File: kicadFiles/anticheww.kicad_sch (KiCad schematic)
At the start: 154 parts, among them J1 TYPE-C-31-M12_13, SW1 ESC, SW10 9, SW11 0, SW12 MINUS, SW13 PLUS, SW14 LBKSP, SW15 RBKSP, SW16 PGUP, SW17 2U_BKSP, SW18 TAB, SW19 Q, SW2 1, SW20 W, SW21 E, SW22 R, SW23 T, SW24 Y, SW25 U, SW26 I, SW27 O, SW28 P, SW29 LBRKT, SW3 2, SW30 RBRKT, SW31 BKSLSH, SW32 PGDN, SW33 CAPS, SW34 A, SW35 S, SW36 D, SW37 F, SW38 G, SW39 H, SW4 3, SW40 J, SW41 K, SW42 L, SW43 COLON, SW44 QUOTE, SW45 ENTER, SW46 HOME, SW47 LSHFT, SW48 STEPPED_CAPS, SW49 Z, SW5 4, SW50 X, SW51 C, SW52 V, SW53 B, SW54 N, SW55 M, SW56 COMMA, SW57 DOT, SW58 175_RSHFT, SW59 UP, SW6 5, SW60 END, SW61 SLSH, SW62 LCTRL, SW63 LGUI, SW64 LALT, SW65 SPC, SW66 RALT, SW67 RGUI, SW68 RCTRL, SW69 LEFT, SW7 6, SW70 DOWN, SW71 RIGHT, SW72 LCTRL, SW73 LGUI, SW74 LALT, SW75 SPC, SW8 7, SW9 8

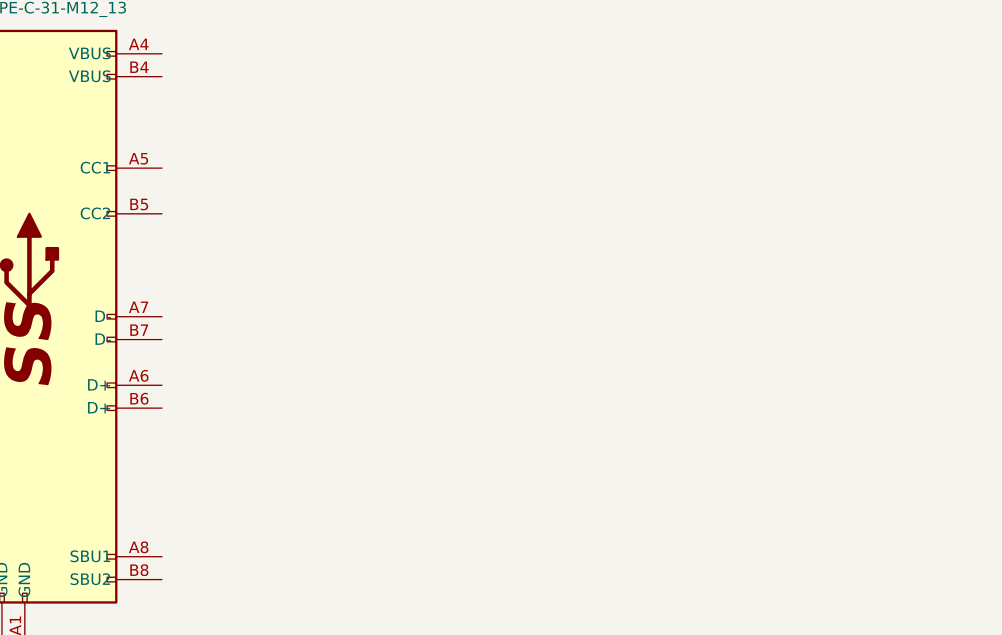
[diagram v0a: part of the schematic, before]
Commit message: Route USB data lines
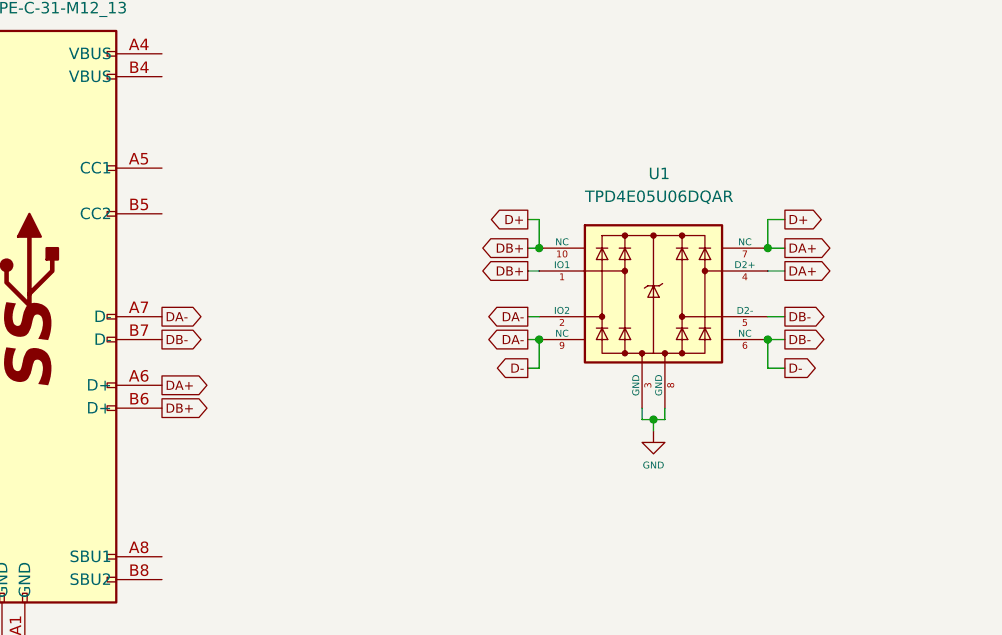
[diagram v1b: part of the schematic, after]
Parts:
- added U1: TPD4E05U06DQAR, acheron_Components:USON-10_2.5x1.0mm_P0.5mm, symbol acheronSymbols:TPD4E05U06DQAR
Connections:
- net GND: now also U1.3 (GND), U1.8 (GND)
- net D+: now reaches J1.A6 (D+)
- net D+: now also J1.B6 (D+), U1.1 (IO1), U1.10 (NC), U1.4 (D2+), U1.7 (NC)
- net D-: now reaches J1.A7 (D-)
- net D-: now also J1.B7 (D-), U1.2 (IO2), U1.5 (D2-), U1.6 (NC), U1.9 (NC)
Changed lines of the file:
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@@
     (title "Anticheww")
     (date "2020-07-03")
-    (rev "V2.0.1")
+    (rev "V2.0.2")
     (company "Designed by Gondolindrim")
     (comment 1 "In partnership with Chewwy")
@@
   (junction (at 127 118.11) (diameter 0) (color 0 0 0 0))
   (junction (at 153.035 548.005) (diameter 0) (color 0 0 0 0))
+  (junction (at 211.455 502.285) (diameter 0) (color 0 0 0 0))
+  (junction (at 211.455 512.445) (diameter 0) (color 0 0 0 0))
+  (junction (at 224.155 521.335) (diameter 0) (color 0 0 0 0))
+  (junction (at 236.855 502.285) (diameter 0) (color 0 0 0 0))
+  (junction (at 236.855 512.445) (diameter 0) (color 0 0 0 0))
   (junction (at 482.6 54.61) (diameter 0) (color 0 0 0 0))
   (wire (pts (xy 118.11 127) (xy 118.11 128.27))
@@
     (stroke (width 0) (type solid) (color 0 0 0 0))
   )
+  (wire (pts (xy 210.185 499.11) (xy 211.455 499.11))
+    (stroke (width 0) (type solid) (color 0 0 0 0))
+  )
+  (wire (pts (xy 210.185 502.285) (xy 211.455 502.285))
+    (stroke (width 0) (type solid) (color 0 0 0 0))
+  )
+  (wire (pts (xy 210.185 504.825) (xy 211.455 504.825))
+    (stroke (width 0) (type solid) (color 0 0 0 0))
+  )
+  (wire (pts (xy 210.185 509.905) (xy 211.455 509.905))
+    (stroke (width 0) (type solid) (color 0 0 0 0))
+  )
+  (wire (pts (xy 210.185 512.445) (xy 211.455 512.445))
+    (stroke (width 0) (type solid) (color 0 0 0 0))
+  )
+  (wire (pts (xy 211.455 499.11) (xy 211.455 502.285))
+    (stroke (width 0) (type solid) (color 0 0 0 0))
+  )
+  (wire (pts (xy 211.455 512.445) (xy 211.455 515.62))
+    (stroke (width 0) (type solid) (color 0 0 0 0))
+  )
+  (wire (pts (xy 211.455 515.62) (xy 210.185 515.62))
+    (stroke (width 0) (type solid) (color 0 0 0 0))
+  )
+  (wire (pts (xy 222.885 520.065) (xy 222.885 521.335))
+    (stroke (width 0) (type solid) (color 0 0 0 0))
+  )
+  (wire (pts (xy 222.885 521.335) (xy 224.155 521.335))
+    (stroke (width 0) (type solid) (color 0 0 0 0))
+  )
+  (wire (pts (xy 224.155 521.335) (xy 224.155 522.605))
+    (stroke (width 0) (type solid) (color 0 0 0 0))
+  )
+  (wire (pts (xy 224.155 521.335) (xy 225.425 521.335))
+    (stroke (width 0) (type solid) (color 0 0 0 0))
+  )
+  (wire (pts (xy 225.425 521.335) (xy 225.425 520.065))
+    (stroke (width 0) (type solid) (color 0 0 0 0))
+  )
   (wire (pts (xy 228.6 44.45) (xy 228.6 45.72))
     (stroke (width 0) (type solid) (color 0 0 0 0))
@@
     (stroke (width 0) (type solid) (color 0 0 0 0))
   )
+  (wire (pts (xy 236.855 499.11) (xy 236.855 502.285))
+    (stroke (width 0) (type solid) (color 0 0 0 0))
+  )
+  (wire (pts (xy 236.855 502.285) (xy 238.76 502.285))
+    (stroke (width 0) (type solid) (color 0 0 0 0))
+  )
+  (wire (pts (xy 236.855 504.825) (xy 238.76 504.825))
+    (stroke (width 0) (type solid) (color 0 0 0 0))
+  )
+  (wire (pts (xy 236.855 509.905) (xy 238.76 509.905))
+    (stroke (width 0) (type solid) (color 0 0 0 0))
+  )
+  (wire (pts (xy 236.855 512.445) (xy 238.76 512.445))
+    (stroke (width 0) (type solid) (color 0 0 0 0))
+  )
+  (wire (pts (xy 236.855 515.62) (xy 236.855 512.445))
+    (stroke (width 0) (type solid) (color 0 0 0 0))
+  )
+  (wire (pts (xy 238.76 499.11) (xy 236.855 499.11))
+    (stroke (width 0) (type solid) (color 0 0 0 0))
+  )
+  (wire (pts (xy 238.76 515.62) (xy 236.855 515.62))
+    (stroke (width 0) (type solid) (color 0 0 0 0))
+  )
   (wire (pts (xy 254 44.45) (xy 254 45.72))
     (stroke (width 0) (type solid) (color 0 0 0 0))
@@
     (effects (font (size 1.27 1.27)) (justify left))
   )
+  (global_label "DA-" (shape output) (at 169.545 509.905 0)
+    (effects (font (size 1.016 1.016)) (justify left))
+  )
+  (global_label "DB-" (shape output) (at 169.545 512.445 0)
+    (effects (font (size 1.016 1.016)) (justify left))
+  )
+  (global_label "DA+" (shape output) (at 169.545 517.525 0)
+    (effects (font (size 1.016 1.016)) (justify left))
+  )
+  (global_label "DB+" (shape output) (at 169.545 520.065 0)
+    (effects (font (size 1.016 1.016)) (justify left))
+  )
+  (global_label "D+" (shape output) (at 210.185 499.11 180)
+    (effects (font (size 1.016 1.016)) (justify right))
+  )
+  (global_label "DB+" (shape output) (at 210.185 502.285 180)
+    (effects (font (size 1.016 1.016)) (justify right))
+  )
+  (global_label "DB+" (shape output) (at 210.185 504.825 180)
+    (effects (font (size 1.016 1.016)) (justify right))
+  )
+  (global_label "DA-" (shape output) (at 210.185 509.905 180)
+    (effects (font (size 1.016 1.016)) (justify right))
+  )
+  (global_label "DA-" (shape output) (at 210.185 512.445 180)
+    (effects (font (size 1.016 1.016)) (justify right))
+  )
+  (global_label "D-" (shape output) (at 210.185 515.62 180)
+    (effects (font (size 1.016 1.016)) (justify right))
+  )
+  (global_label "D+" (shape output) (at 238.76 499.11 0)
+    (effects (font (size 1.016 1.016)) (justify left))
+  )
+  (global_label "DA+" (shape output) (at 238.76 502.285 0)
+    (effects (font (size 1.016 1.016)) (justify left))
+  )
+  (global_label "DA+" (shape output) (at 238.76 504.825 0)
+    (effects (font (size 1.016 1.016)) (justify left))
+  )
+  (global_label "DB-" (shape output) (at 238.76 509.905 0)
+    (effects (font (size 1.016 1.016)) (justify left))
+  )
+  (global_label "DB-" (shape output) (at 238.76 512.445 0)
+    (effects (font (size 1.016 1.016)) (justify left))
+  )
+  (global_label "D-" (shape output) (at 238.76 515.62 0)
+    (effects (font (size 1.016 1.016)) (justify left))
+  )
   (symbol (lib_id "power:GND") (at 153.035 549.275 0) (unit 1)
     (in_bom yes) (on_board yes)
@@
     )
   )
+  (symbol (lib_id "power:GND") (at 224.155 522.605 0) (unit 1)
+    (in_bom yes) (on_board yes)
+    (property "Reference" "#PWR0102" (id 0) (at 224.155 528.955 0)
+      (effects (font (size 1.27 1.27)) hide)
+    )
+    (property "Value" "GND" (id 1) (at 224.155 526.415 0)
+      (effects (font (size 0.762 0.762)))
+    )
+    (property "Footprint" "" (id 2) (at 224.155 522.605 0)
+      (effects (font (size 1.27 1.27)) hide)
+    )
+    (property "Datasheet" "" (id 3) (at 224.155 522.605 0)
+      (effects (font (size 1.27 1.27)) hide)
+    )
+  )
   (symbol (lib_id "Mechanical:MountingHole") (at 71.12 495.935 0) (unit 1)
     (in_bom no) (on_board yes)
@@
     )
   )
+  (symbol (lib_id "acheronSymbols:TPD4E05U06DQAR") (at 224.155 507.365 0) (unit 1)
+    (in_bom yes) (on_board yes)
+    (property "Reference" "U1" (id 0) (at 224.79 494.03 0))
+    (property "Value" "TPD4E05U06DQAR" (id 1) (at 224.79 496.57 0))
+    (property "Footprint" "acheron_Components:USON-10_2.5x1.0mm_P0.5mm" (id 2) (at 224.155 480.695 0)
+      (effects (font (size 1.27 1.27)) hide)
+    )
+    (property "Datasheet" "" (id 3) (at 224.155 507.365 0)
+      (effects (font (size 1.27 1.27)) hide)
+    )
+    (property "Manufacturer" "Texas Instruments" (id 4) (at 224.155 483.235 0)
+      (effects (font (size 1.27 1.27)) hide)
+    )
+    (property "Package" "uSON-10" (id 7) (at 224.155 485.775 0)
+      (effects (font (size 1.27 1.27)) hide)
+    )
+    (property "Manufacturer Part Number" "TPD4E05U06DQAR" (id 4) (at 224.155 507.365 0)
+      (effects (font (size 1.27 1.27)) hide)
+    )
+    (property "LCSC Part Number" "C138714" (id 5) (at 224.155 507.365 0)
+      (effects (font (size 1.27 1.27)) hide)
+    )
+  )
   (symbol (lib_id "acheronSymbols:TYPE-C-31-M12_13") (at 154.305 509.905 0) (unit 1)
     (in_bom yes) (on_board yes)
@@
       (reference "#PWR0101") (unit 1)
     )
+    (path "/2ca7166e-cb5d-4fa3-b1b6-95a762aabfb3"
+      (reference "#PWR0102") (unit 1)
+    )
     (path "/543a7d54-a886-4795-b487-5ed8576a1063"
       (reference "D1") (unit 1)
@@
       (reference "SW75") (unit 1)
     )
+    (path "/155bad83-d77a-43be-9512-7c5efecea63e"
+      (reference "U1") (unit 1)
+    )
   )

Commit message: Add RGB
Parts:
- added C1, C10, C11, C12, C13, C14, C2, C3, C4, C5, C6, C7, C8, C9: 100n, Capacitor_SMD:C_0805_2012Metric, symbol Device:C
- added D47: 1N4148W, acheron_Components:D_SOD-123, symbol Device:D
- added D71, D72, D73, D74, D75, D76, D77, D78, D79, D80, D81, D82, D83, D84: WS2812C, acheron_Components:LED_WS2812B_5.0x5.0mm_P3.2mm, symbol LED:WS2812B
- added FB1, FB2: CBG201209U121T, Inductor_SMD:L_0805_2012Metric, symbol Device:Ferrite_Bead_Small
- added GR1: Warning Sign (ISO Enter + LED), acheron_Graphics:warning_sign_3.6x3.2mm, symbol Mechanical:MountingHole
- added GR2: Warning Sign (Backspace), acheron_Graphics:warning_sign_3.6x3.2mm, symbol Mechanical:MountingHole
- added GR3: Warning Sign (ANSI Enter + ISO Backslash), acheron_Graphics:warning_sign_3.6x3.2mm, symbol Mechanical:MountingHole
- added GR4: Warning Sign (7U Space), acheron_Graphics:warning_sign_3.6x3.2mm, symbol Mechanical:MountingHole
- added GR5: Warning Sign (Left shift), acheron_Graphics:warning_sign_3.6x3.2mm, symbol Mechanical:MountingHole
- added LED1, LED10, LED11, LED12, LED13, LED14, LED15, LED16, LED17, LED18, LED19, LED2, LED20, LED21, LED22, LED23, LED24, LED25, LED26, LED27, LED28, LED29, LED3, LED30, LED31, LED32, LED33, LED34, LED35, LED36, LED37, LED38, LED39, LED4, LED40, LED41, LED42, LED43, LED44, LED45, LED46, LED47, LED48, LED49, LED5, LED50, LED51, LED52, LED53, LED54, LED55, LED56, LED57, LED58, LED59, LED6, LED60, LED61, LED62, LED63, LED64, LED65, LED66, LED67, LED68, LED69, LED7, LED70, LED71, LED72, LED73, LED74, LED75, LED76, LED77, LED78, LED79, LED8, LED80, LED9: LED, acheron_Components:LED_THT_2.54mm, symbol acheronSymbols:LED
- added Q1: AO3401A, Package_TO_SOT_SMD:SOT-23, symbol Transistor_FET:AO3401A
- added Q2: DTC123JKAT146, Package_TO_SOT_SMD:SOT-23, symbol acheronSymbols:DTC123J
- added R1: 1k, Resistor_SMD:R_0805_2012Metric, symbol Device:R
- added R10, R11, R12, R13, R14, R15, R16, R17, R18, R19, R20, R21, R22, R23, R24, R25, R33, R34, R35, R36, R37, R38, R39, R40, R41, R42, R43, R44, R45, R46, R47, R48, R49, R50, R51, R52, R53, R54, R55, R56, R57, R58, R59, R60, R61, R62, R63, R64, R65, R66, R67, R68, R69, R70, R71, R72, R73, R74, R75, R76, R77, R78, R79, R80, R81, R82, R83, R84, R85, R86, R87, R88, R89: 420R, Resistor_SMD:R_0805_2012Metric, symbol Device:R
- added R2: 100R, Resistor_SMD:R_0805_2012Metric, symbol Device:R
- added R26, R27, R28, R29, R3, R30, R31, R32, R4, R5, R6, R7, R8, R9: 5R, Resistor_SMD:R_0805_2012Metric, symbol Device:R
- added R90, R91: 5.1k, Resistor_SMD:R_0805_2012Metric, symbol Device:R
- added SW32: ISO_ENTER, acheron_MX_SolderMask:MX_ISOEnter_Vertical_LED, symbol acheronSymbols:MXSwitch
- added SW49: ISO_TILDE, acheron_MX_SolderMask:MX100, symbol acheronSymbols:MXSwitch
- added SW51: ISO_BKLSH, acheron_MX_SolderMask:MX100, symbol acheronSymbols:MXSwitch
- added SW65: ISO_LSHFT, acheron_MX_SolderMask:MX125, symbol acheronSymbols:MXSwitch
- H1: renamed from H2; symbol Mechanical:MountingHole -> Mechanical:MountingHole_Pad
- H7: renamed from H8; symbol Mechanical:MountingHole_Pad -> Mechanical:MountingHole
- SW45: footprint acheron_MX_SolderMask:MX225R -> acheron_MX_SolderMask:MX225
- U1: Manufacturer Texas Instruments -> (none); Package uSON-10 -> (none)
- renumbered D17 to D16, D18 to D17, D19 to D18, D20 to D19, D21 to D20, D22 to D21, D23 to D22, D24 to D23, D25 to D24, D26 to D25, D27 to D26, D28 to D27, D29 to D28, D30 to D29, D31 to D30, D32 to D31, D33 to D32, D34 to D33, D35 to D34, D36 to D35, D37 to D36, D38 to D37, D39 to D38, D40 to D39, D41 to D40, D42 to D41, D43 to D42, D44 to D43, D45 to D44, D16 to D45, D47 to D48, D48 to D49, D49 to D50, D50 to D51, D51 to D52, D52 to D53, D53 to D54, D54 to D55, D55 to D56, D59 to D57, D56 to D58, D57 to D59, D58 to D60, D60 to D61, D61 to D62, D62 to D63, D63 to D64, D64 to D65, D65 to D66, D66 to D67, D67 to D68, D68 to D69, D69 to D70, H3 to H2, H4 to H3, H5 to H4, H6 to H5, H7 to H6, H9 to H8, H10 to H9, SW17 to SW16, SW18 to SW17, SW19 to SW18, SW20 to SW19, SW21 to SW20, SW22 to SW21, SW23 to SW22, SW24 to SW23, SW25 to SW24, SW26 to SW25, SW27 to SW26, SW28 to SW27, SW29 to SW28, SW30 to SW29, SW31 to SW30, SW32 to SW31, SW16 to SW47, SW47 to SW50, SW49 to SW52, SW50 to SW53, SW51 to SW54, SW52 to SW55, SW53 to SW56, SW54 to SW57, SW55 to SW58, SW56 to SW59, SW57 to SW60, SW58 to SW62, SW59 to SW63, SW60 to SW64, SW62 to SW66, SW63 to SW67, SW64 to SW68, SW65 to SW69, SW66 to SW70, SW67 to SW71, SW68 to SW72, SW69 to SW73, SW70 to SW74, SW71 to SW75, SW72 to SW76, SW73 to SW77, SW74 to SW78, SW75 to SW79
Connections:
- net CASE: now also H1.1, FB1.2; no longer H7.1
- net GND: now also C1.1, C10.1, C11.1, C12.1, C13.1, C14.1, C2.1, C3.1, C4.1, C5.1, C6.1, C7.1, C8.1, C9.1, D71.3 (VSS), D72.3 (VSS), D73.3 (VSS), D74.3 (VSS), D75.3 (VSS), D76.3 (VSS), D77.3 (VSS), D78.3 (VSS), D79.3 (VSS), D80.3 (VSS), D81.3 (VSS), D82.3 (VSS), D83.3 (VSS), D84.3 (VSS), FB1.1, FB2.1, LED1.K, LED10.K, LED11.K, LED12.K, LED13.K, LED14.K, LED15.K, LED16.K, LED17.K, LED18.K, LED19.K, LED2.K, LED20.K, LED21.K, LED22.K, LED23.K, LED24.K, LED25.K, LED26.K, LED27.K, LED28.K, LED29.K, LED3.K, LED30.K, LED31.K, LED32.K, LED33.K, LED34.K, LED35.K, LED36.K, LED37.K, LED38.K, LED39.K, LED4.K, LED40.K, LED41.K, LED42.K, LED43.K, LED44.K, LED45.K, LED46.K, LED47.K, LED48.K, LED49.K, LED5.K, LED50.K, LED51.K, LED52.K, LED53.K, LED54.K, LED55.K, LED56.K, LED57.K, LED58.K, LED59.K, LED6.K, LED60.K, LED61.K, LED62.K, LED63.K, LED64.K, LED65.K, LED66.K, LED67.K, LED68.K, LED69.K, LED7.K, LED70.K, LED71.K, LED72.K, LED73.K, LED74.K, LED75.K, LED76.K, LED77.K, LED78.K, LED79.K, LED8.K, LED80.K, LED9.K, Q2.2 (E), R90.2, R91.2
- net at D5.1 (K): now also D1.1 (K), D10.1 (K), D11.1 (K), D12.1 (K), D13.1 (K), D14.1 (K), D15.1 (K), D2.1 (K), D3.1 (K), D4.1 (K), D6.1 (K), D7.1 (K), D8.1 (K), D9.1 (K)
- net at SW18.1 (Col): now also SW2.1 (Col), SW34.1 (Col), SW67.1 (Col), SW77.1 (Col), SW51.1 (Col)
- net at D17.1 (K): now also D16.1 (K), D18.1 (K), D19.1 (K), D20.1 (K), D21.1 (K), D22.1 (K), D23.1 (K), D24.1 (K), D25.1 (K), D26.1 (K), D27.1 (K), D28.1 (K), D29.1 (K), D30.1 (K)
- net at SW14.1 (Col): now also SW30.1 (Col), SW46.1 (Col), SW63.1 (Col), SW74.1 (Col), SW32.1 (Col)
- net at D31.1 (K): now also D32.1 (K), D33.1 (K), D34.1 (K), D35.1 (K), D36.1 (K), D37.1 (K), D38.1 (K), D39.1 (K), D40.1 (K), D41.1 (K), D42.1 (K), D43.1 (K), D44.1 (K), D45.1 (K)
- net at SW78.1 (Col): now also SW19.1 (Col), SW3.1 (Col), SW35.1 (Col), SW52.1 (Col), SW68.1 (Col)
- net S3: now reaches SW78.2 (Row)
- net S3: now also D63.2 (A), SW68.2 (Row)
- net at SW22.1 (Col): now also SW38.1 (Col), SW55.1 (Col), SW6.1 (Col), SW69.1 (Col), SW79.1 (Col)
- net at D29.2 (A), SW30.2 (Row): now also SW32.2 (Row)
- net at SW12.1 (Col): now also SW28.1 (Col), SW44.1 (Col), SW61.1 (Col), SW72.1 (Col)
- net at SW75.1 (Col): now also SW15.1 (Col), SW16.1 (Col), SW31.1 (Col), SW47.1 (Col), SW64.1 (Col)
- net at SW56.1 (Col): now also SW23.1 (Col), SW39.1 (Col), SW7.1 (Col)
- net at SW24.1 (Col): now also SW40.1 (Col), SW57.1 (Col), SW8.1 (Col)
- net at SW27.1 (Col): now also SW11.1 (Col), SW43.1 (Col), SW60.1 (Col), SW71.1 (Col)
- net at D70.1 (K): now also D61.1 (K), D62.1 (K), D63.1 (K), D64.1 (K), D65.1 (K), D66.1 (K), D67.1 (K), D68.1 (K), D69.1 (K)
- net at D48.1 (K): now also D46.1 (K), D49.1 (K), D50.1 (K), D51.1 (K), D52.1 (K), D53.1 (K), D54.1 (K), D55.1 (K), D56.1 (K), D57.1 (K), D58.1 (K), D59.1 (K), D60.1 (K), D47.1 (K)
- net at SW37.1 (Col): now also SW21.1 (Col), SW5.1 (Col), SW54.1 (Col)
- net S4: now reaches SW79.2 (Row)
- net S4: now also D64.2 (A), SW69.2 (Row)
- net VBUS: now reaches J1.A4 (VBUS)
- net VBUS: now also J1.B4 (VBUS)
- net at J1.A5 (CC1): now also R90.1
- net at J1.B5 (CC2): now also R91.1
- net at J1.S (SHIELD): now also FB2.2
- net at SW25.1 (Col): now also SW41.1 (Col), SW58.1 (Col), SW9.1 (Col)
- net S2: now reaches SW77.2 (Row)
- net S2: now also D62.2 (A), SW67.2 (Row)
- net at SW29.1 (Col): now also SW13.1 (Col), SW45.1 (Col), SW62.1 (Col), SW73.1 (Col), SW49.1 (Col)
- net at SW4.1 (Col): now also SW20.1 (Col), SW36.1 (Col), SW53.1 (Col)
- net S1: now reaches D61.2 (A), SW66.2 (Row)
- net S1: now also SW76.2 (Row)
- net at SW66.1 (Col): now also SW1.1 (Col), SW17.1 (Col), SW33.1 (Col), SW48.1 (Col), SW50.1 (Col), SW76.1 (Col), SW65.1 (Col)
- net at SW70.1 (Col): now also SW10.1 (Col), SW26.1 (Col), SW42.1 (Col), SW59.1 (Col)
- net at D46.2 (A), SW50.2 (Row): now also SW65.2 (Row)
- net at D43.2 (A), SW45.2 (Row): now also SW49.2 (Row)
- new net: LED61.A, R74.1
- new net: Q1.3 (D), R10.2, R11.2, R12.2, R13.2, R14.2, R15.2, R16.2, R17.2, R18.2, R19.2, R20.2, R21.2, R22.2, R23.2, R24.2, R25.2, R33.2, R34.2, R35.2, R36.2, R37.2, R38.2, R39.2, R40.2, R41.2, R42.2, R43.2, R44.2, R45.2, R46.2, R47.2, R48.2, R49.2, R50.2, R51.2, R52.2, R53.2, R54.2, R55.2, R56.2, R57.2, R58.2, R59.2, R60.2, R61.2, R62.2, R63.2, R64.2, R65.2, R66.2, R67.2, R68.2, R69.2, R70.2, R71.2, R72.2, R73.2, R74.2, R75.2, R76.2, R77.2, R78.2, R79.2, R80.2, R81.2, R82.2, R83.2, R84.2, R85.2, R86.2, R87.2, R88.2, R89.2
- new net: LED48.A, R62.1
- new net: LED7.A, R16.1
- new net: LED19.A, R34.1
- new net: LED14.A, R23.1
- new net: C2.2, D72.1 (VDD), R4.1
- new net: LED46.A, R60.1
- new net: C14.2, D84.1 (VDD), R32.1
- new net: LED37.A, R51.1
- new net: C7.2, D77.1 (VDD), R9.1
- new net: C5.2, D75.1 (VDD), R7.1
- new net: LED33.A, LED34.A, R48.1
- new net: LED60.A, R73.1
- new net: LED30.A, R45.1
- new net: D72.2 (DOUT), D73.4 (DIN)
- new net: D71.2 (DOUT), D72.4 (DIN)
- new net: LED31.A, R46.1
- new net: LED39.A, R53.1
- new net: LED15.A, LED16.A, R24.1
- new net: LED43.A, R57.1
- new net: LED57.A, R70.1
- new net: LED17.A, R25.1
- new net: LED67.A, LED68.A, R79.1
- new net: LED65.A, LED66.A, R78.1
- new net: LED78.A, R87.1
- new net: LED22.A, R37.1
- new net: C10.2, D80.1 (VDD), R28.1
- new net: D79.4 (DIN), D80.2 (DOUT)
- new net: D80.4 (DIN), D81.2 (DOUT)
- new net: LED53.A, R66.1
- new net: Q2.3 (C), R1.2, R2.2
- new net: LED6.A, R15.1
- new net: LED74.A, R83.1
- new net: LED18.A, R33.1
- new net: LED62.A, R75.1
- new net: LED69.A, LED70.A, R80.1
- new net: LED10.A, R19.1
- new net: LED27.A, R42.1
- new net: LED29.A, R44.1
- new net: C8.2, D78.1 (VDD), R26.1
- new net: D78.4 (DIN), D79.2 (DOUT)
- new net: LED8.A, R17.1
- new net: C13.2, D83.1 (VDD), R31.1
- new net: C3.2, D73.1 (VDD), R5.1
- new net: LED71.A, LED72.A, R81.1
- new net: LED80.A, R89.1
- new net: LED44.A, R58.1
- new net: LED24.A, R39.1
- new net: Q1.1 (G), R2.1
- new net: LED4.A, R13.1
- new net: LED9.A, R18.1
- new net: LED77.A, R86.1
- new net: LED59.A, R72.1
- new net: LED23.A, R38.1
- new net: LED45.A, R59.1
- new net: LED40.A, R54.1
- new net: C12.2, D82.1 (VDD), R30.1
- new net: D81.4 (DIN), D82.2 (DOUT)
- new net: D82.4 (DIN), D83.2 (DOUT)
- new net: LED3.A, R12.1
- new net: LED26.A, R41.1
- new net: LED54.A, R67.1
- new net: LED55.A, R68.1
- new net: C11.2, D81.1 (VDD), R29.1
- new net: D83.4 (DIN), D84.2 (DOUT)
- new net: D77.2 (DOUT), D84.4 (DIN)
- new net: LED56.A, R69.1
- new net: LED11.A, R20.1
- new net: LED25.A, R40.1
- new net: LED49.A, LED50.A, R63.1
- new net: LED64.A, R77.1
- new net: LED42.A, R56.1
- new net: C6.2, D76.1 (VDD), R8.1
- new net: LED5.A, R14.1
- new net: LED32.A, R47.1
- new net: C9.2, D79.1 (VDD), R27.1
- new net: LED73.A, R82.1
- new net: LED79.A, R88.1
- new net: D76.2 (DOUT), D77.4 (DIN)
- new net: D75.2 (DOUT), D76.4 (DIN)
- new net: LED52.A, R65.1
- new net: LED47.A, R61.1
- new net: LED58.A, R71.1
- new net: LED36.A, R50.1
- new net: D47.2 (A), SW51.2 (Row)
- new net: LED75.A, R84.1
- new net: C4.2, D74.1 (VDD), R6.1
- new net: C1.2, D71.1 (VDD), R3.1
- new net: LED41.A, R55.1
- new net: LED63.A, R76.1
- new net: LED38.A, R52.1
- new net: LED1.A, R10.1
- new net: LED21.A, R36.1
- new net: LED13.A, R22.1
- new net: LED51.A, R64.1
- new net: LED35.A, R49.1
- new net: LED20.A, R35.1
- new net: LED12.A, R21.1
- new net: D74.2 (DOUT), D75.4 (DIN)
- new net: D73.2 (DOUT), D74.4 (DIN)
- new net: LED28.A, R43.1
- new net: LED2.A, R11.1
- new net: LED76.A, R85.1
- new net 5V: Q1.2 (S), R1.1, R26.2, R27.2, R28.2, R29.2, R3.2, R30.2, R31.2, R32.2, R4.2, R5.2, R6.2, R7.2, R8.2, R9.2
- new net RGB_5V: D71.4 (DIN)
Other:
- moved on the sheet: D48, D49, D50, D51, D52, D53, D54, D55, D56, D57, D58, D59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

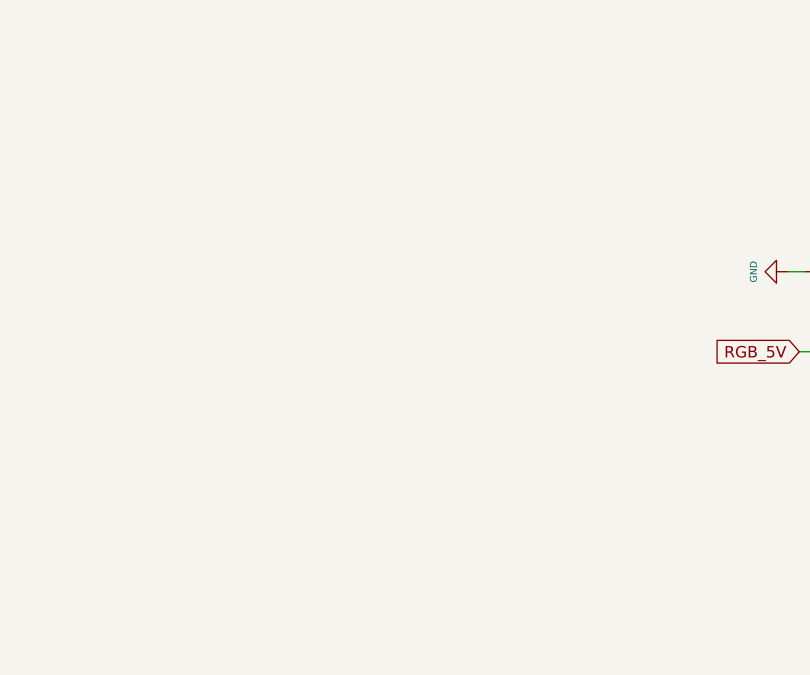
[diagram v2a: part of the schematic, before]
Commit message: Added RGB level translator
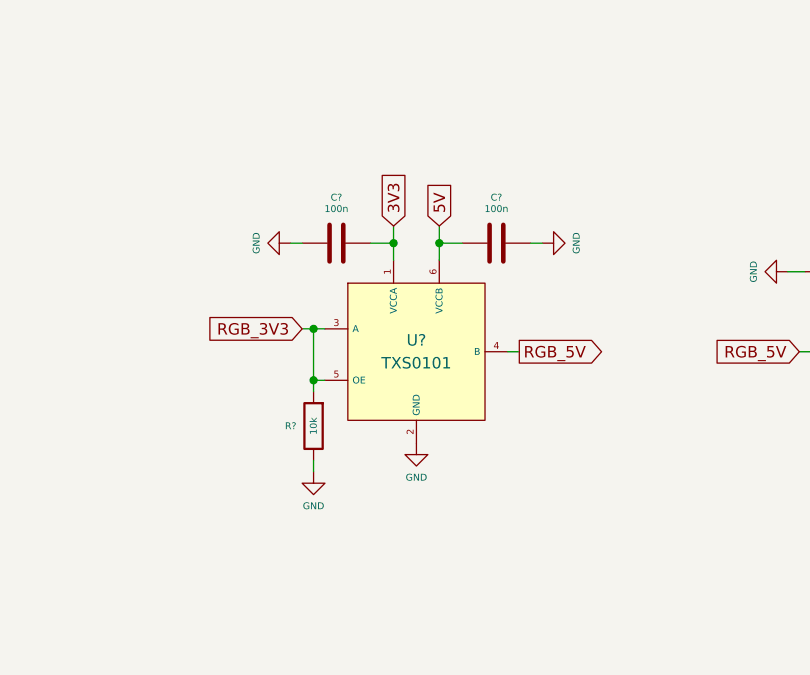
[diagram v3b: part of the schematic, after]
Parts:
- added C? (x2): 100n, Capacitor_SMD:C_0805_2012Metric, symbol Device:C
- added R?: 10k, Resistor_SMD:R_0805_2012Metric, symbol Device:R
- added U?: TXS0101, acheron_Components:SOT-23-6, symbol acheronSymbols:TXS0101
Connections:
- net 5V: now also C?.1, U?.6 (VCCB)
- net GND: now also C?.1, C?.2, R?.1, U?.2 (GND)
- net RGB_5V: now also U?.4 (B)
- new net 3V3: C?.2, U?.1 (VCCA)
- new net RGB_3V3: R?.2, U?.3 (A), U?.5 (OE)
